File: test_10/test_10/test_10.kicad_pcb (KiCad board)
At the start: 2 copper layers, 100 x 100 mm, 184 parts, among them J2 Array set 0

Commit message: renumber
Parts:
- renumbered H11 to H10, H12 to H11, H13 to H12, H8 to H7, H9 to H8, H10 to H9, J2 to J1, LS49 to LS10, LS21 to LS11, LS22 to LS12, LS23 to LS13, LS24 to LS14, LS25 to LS15, LS26 to LS16, LS27 to LS17, LS28 to LS18, LS50 to LS19, LS30 to LS20, LS11 to LS21, LS12 to LS22, LS13 to LS23, LS14 to LS24, LS15 to LS25, LS16 to LS26, LS17 to LS27, LS18 to LS28, LS19 to LS29, LS20 to LS30, LS41 to LS31, LS80 to LS32, LS47 to LS37, LS48 to LS38, LS51 to LS41, LS52 to LS42, LS53 to LS43, LS54 to LS44, LS55 to LS45, LS56 to LS46, LS57 to LS47, LS58 to LS48, LS59 to LS49, LS60 to LS50, LS71 to LS51, LS72 to LS52, LS73 to LS53, LS74 to LS54, LS75 to LS55, LS79 to LS56, LS78 to LS57, R3 to R1, R12 to R10, R120 to R100, R141 to R101, R142 to R102, R143 to R103, R144 to R104, R145 to R105, R146 to R106, R147 to R107, R151 to R108, R152 to R109, R23 to R11, R153 to R110, R154 to R111, R155 to R112, R156 to R113, R157 to R114, R24 to R12, R25 to R13, R26 to R14, R27 to R15, R28 to R16, R29 to R17, R30 to R18, R31 to R19, R4 to R2, R32 to R20, R43 to R21, R44 to R22, R45 to R23, R46 to R24, R47 to R25, R48 to R26, R49 to R27, R50 to R28, R51 to R29, R5 to R3, R52 to R30, R63 to R31, R64 to R32, R65 to R33, R66 to R34, R67 to R35, R68 to R36, R69 to R37, R70 to R38, R71 to R39, R6 to R4, R72 to R40, R1 to R41, R2 to R42, R13 to R43, R14 to R44, R15 to R45, R16 to R46, R17 to R47, R18 to R48, R19 to R49, R7 to R5, R20 to R50, R21 to R51, R22 to R52, R33 to R53, R34 to R54, R35 to R55, R36 to R56, R37 to R57, R38 to R58, R39 to R59, R8 to R6, R40 to R60, R41 to R61, R42 to R62, R53 to R63, R54 to R64, R55 to R65, R56 to R66, R57 to R67, R58 to R68, R59 to R69, R9 to R7, R60 to R70, R61 to R71, R62 to R72, R10 to R8, R101 to R81, R102 to R82, R103 to R83, R104 to R84, R105 to R85, R106 to R86, R107 to R87, R108 to R88, R109 to R89, R11 to R9, R110 to R90, R111 to R91, R112 to R92, R113 to R93, R114 to R94, R115 to R95, R116 to R96, R117 to R97, R118 to R98, R119 to R99

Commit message: pcb finish
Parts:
- added D1: LED, temp_pcb_lib:CREE_CXB1512, F.Cu at (400.0, 250.0)
- added J2: Array set 0, Connector_Phoenix_MC:PhoenixContact_MCV_1,5_2-G-3.5_1x02_P3.50mm_Vertical, F.Cu at (360.8, 242.0)
- added LS58: Ultrasonic, temp_pcb_lib:Buzzer_MSO-A1040H07T_D10mm_H7mm, F.Cu at (386.1, 285.3)
- added LS59: Ultrasonic, temp_pcb_lib:Buzzer_MSO-A1040H07T_D10mm_H7mm, F.Cu at (375.1, 285.6)
- added R115: 0.1Ω, Resistor_SMD:R_0603_1608Metric, F.Cu at (386.9, 283.0)
- added R116: 0.1Ω, Resistor_SMD:R_0603_1608Metric, F.Cu at (390.3, 288.0)
- added R117: 0.1Ω, Resistor_SMD:R_0603_1608Metric, F.Cu at (375.9, 283.1)
- added R118: 0.1Ω, Resistor_SMD:R_0603_1608Metric, F.Cu at (379.3, 288.4)
- moved R108 174.4 mm to (436.1, 252.5), turned to 180 degrees
- moved R79 172.9 mm to (441.9, 243.6), turned to 180 degrees
- moved R101 172.0 mm to (432.8, 247.4)
- moved R55 167.1 mm to (418.9, 225.9), turned to 180 degrees
- moved R103 166.3 mm to (415.7, 256.2)
- moved R20 162.6 mm to (418.9, 278.8), turned to 180 degrees
- moved R97 157.8 mm to (413.1, 217.1), turned to 180 degrees
- moved R54 157.6 mm to (413.1, 234.7), turned to 180 degrees
- moved R5 152.9 mm to (421.3, 282.9)
- moved R60 152.7 mm to (413.2, 288.0), turned to 180 degrees
- moved R110 151.4 mm to (418.9, 261.2), turned to 180 degrees
- moved R99 149.6 mm to (390.1, 234.7), turned to 180 degrees
- moved R81 148.4 mm to (421.3, 212.1)
- moved R45 146.9 mm to (415.5, 221.0)
- moved R100 146.8 mm to (395.9, 208.0), turned to 180 degrees
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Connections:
- J1 pad 2: Net-(J1-Pad1) -> Net-(J1-Pad2)
- R1 pad 2: Net-(J1-Pad1) -> Net-(J1-Pad2)
- R10 pad 2: Net-(J1-Pad1) -> Net-(J1-Pad2)
- R101 pad 2: Net-(J1-Pad1) -> Net-(J1-Pad2)
- R102 pad 2: Net-(J1-Pad1) -> Net-(J1-Pad2)
- R103 pad 2: Net-(J1-Pad1) -> Net-(J1-Pad2)
- R104 pad 2: Net-(J1-Pad1) -> Net-(J1-Pad2)
- R105 pad 2: Net-(J1-Pad1) -> Net-(J1-Pad2)
- R106 pad 2: Net-(J1-Pad1) -> Net-(J1-Pad2)
- R107 pad 2: Net-(J1-Pad1) -> Net-(J1-Pad2)
- R2 pad 2: Net-(J1-Pad1) -> Net-(J1-Pad2)
- R21 pad 2: Net-(J1-Pad1) -> Net-(J1-Pad2)
- R22 pad 2: Net-(J1-Pad1) -> Net-(J1-Pad2)
- R23 pad 2: Net-(J1-Pad1) -> Net-(J1-Pad2)
- R24 pad 2: Net-(J1-Pad1) -> Net-(J1-Pad2)
- R25 pad 2: Net-(J1-Pad1) -> Net-(J1-Pad2)
- R26 pad 2: Net-(J1-Pad1) -> Net-(J1-Pad2)
- R27 pad 2: Net-(J1-Pad1) -> Net-(J1-Pad2)
- R28 pad 2: Net-(J1-Pad1) -> Net-(J1-Pad2)
- R29 pad 2: Net-(J1-Pad1) -> Net-(J1-Pad2)
- R3 pad 2: Net-(J1-Pad1) -> Net-(J1-Pad2)
- R30 pad 2: Net-(J1-Pad1) -> Net-(J1-Pad2)
- R4 pad 2: Net-(J1-Pad1) -> Net-(J1-Pad2)
- R41 pad 2: Net-(J1-Pad1) -> Net-(J1-Pad2)
- R42 pad 2: Net-(J1-Pad1) -> Net-(J1-Pad2)
- R43 pad 2: Net-(J1-Pad1) -> Net-(J1-Pad2)
- R44 pad 2: Net-(J1-Pad1) -> Net-(J1-Pad2)
- R45 pad 2: Net-(J1-Pad1) -> Net-(J1-Pad2)
- R46 pad 2: Net-(J1-Pad1) -> Net-(J1-Pad2)
- R47 pad 2: Net-(J1-Pad1) -> Net-(J1-Pad2)
- R48 pad 2: Net-(J1-Pad1) -> Net-(J1-Pad2)
- R49 pad 2: Net-(J1-Pad1) -> Net-(J1-Pad2)
- R5 pad 2: Net-(J1-Pad1) -> Net-(J1-Pad2)
- R50 pad 2: Net-(J1-Pad1) -> Net-(J1-Pad2)
- R6 pad 2: Net-(J1-Pad1) -> Net-(J1-Pad2)
- R61 pad 2: Net-(J1-Pad1) -> Net-(J1-Pad2)
- R62 pad 2: Net-(J1-Pad1) -> Net-(J1-Pad2)
- R63 pad 2: Net-(J1-Pad1) -> Net-(J1-Pad2)
- R64 pad 2: Net-(J1-Pad1) -> Net-(J1-Pad2)
- R65 pad 2: Net-(J1-Pad1) -> Net-(J1-Pad2)
- R66 pad 2: Net-(J1-Pad1) -> Net-(J1-Pad2)
- R67 pad 2: Net-(J1-Pad1) -> Net-(J1-Pad2)
- R68 pad 2: Net-(J1-Pad1) -> Net-(J1-Pad2)
- R69 pad 2: Net-(J1-Pad1) -> Net-(J1-Pad2)
- R7 pad 2: Net-(J1-Pad1) -> Net-(J1-Pad2)
- R70 pad 2: Net-(J1-Pad1) -> Net-(J1-Pad2)
- R8 pad 2: Net-(J1-Pad1) -> Net-(J1-Pad2)
- R81 pad 2: Net-(J1-Pad1) -> Net-(J1-Pad2)
- R82 pad 2: Net-(J1-Pad1) -> Net-(J1-Pad2)
- R83 pad 2: Net-(J1-Pad1) -> Net-(J1-Pad2)
- R84 pad 2: Net-(J1-Pad1) -> Net-(J1-Pad2)
- R85 pad 2: Net-(J1-Pad1) -> Net-(J1-Pad2)
- R86 pad 2: Net-(J1-Pad1) -> Net-(J1-Pad2)
- R87 pad 2: Net-(J1-Pad1) -> Net-(J1-Pad2)
- R88 pad 2: Net-(J1-Pad1) -> Net-(J1-Pad2)
- R89 pad 2: Net-(J1-Pad1) -> Net-(J1-Pad2)
- R9 pad 2: Net-(J1-Pad1) -> Net-(J1-Pad2)
- R90 pad 2: Net-(J1-Pad1) -> Net-(J1-Pad2)
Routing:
- net Net-(J1-Pad2): track 0.00 -> 81.0 mm, vias 0 -> 59
- net Net-(D1-Pad1): track 0.00 -> 55.3 mm
- net Net-(D1-Pad2): track 0.00 -> 34.5 mm
- net Net-(LS59-Pad2): track 0.00 -> 2.81 mm
- net Net-(LS38-Pad1): track 0.00 -> 2.76 mm
- net Net-(LS37-Pad2): track 0.00 -> 2.76 mm
- net Net-(LS30-Pad2): track 0.00 -> 2.76 mm
- net Net-(LS58-Pad2): track 0.00 -> 2.71 mm
- net Net-(LS50-Pad1): track 0.00 -> 2.71 mm
- net Net-(LS13-Pad1): track 0.00 -> 2.71 mm
- net Net-(LS5-Pad2): track 0.00 -> 2.70 mm
- net Net-(LS28-Pad1): track 0.00 -> 2.68 mm
- net Net-(LS21-Pad1): track 0.00 -> 2.68 mm
- net Net-(LS15-Pad1): track 0.00 -> 2.68 mm
- net Net-(LS29-Pad1): track 0.00 -> 2.63 mm
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- added copper zone on F.Cu, net Net-(J1-Pad1)
- added copper zone on B.Cu, net Net-(J1-Pad2)

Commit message: 3 trans mas
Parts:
- added LS60: Ultrasonic, temp_pcb_lib:Buzzer_MSO-A1040H07T_D10mm_H7mm, F.Cu at (391.8, 294.1)
- added LS61: Ultrasonic, temp_pcb_lib:Buzzer_MSO-A1040H07T_D10mm_H7mm, F.Cu at (403.3, 294.1)
- added LS62: Ultrasonic, temp_pcb_lib:Buzzer_MSO-A1040H07T_D10mm_H7mm, F.Cu at (358.3, 240.5)
- added R119: 0.1Ω, Resistor_SMD:R_0603_1608Metric, F.Cu at (392.7, 291.6)
- added R120: 0.1Ω, Resistor_SMD:R_0603_1608Metric, F.Cu at (404.2, 291.6)
- added R121: 0.1Ω, Resistor_SMD:R_0603_1608Metric, F.Cu at (359.1, 237.9)
- added R122: 0.1Ω, Resistor_SMD:R_0603_1608Metric, F.Cu at (397.6, 291.6)
- added R123: 0.1Ω, Resistor_SMD:R_0603_1608Metric, F.Cu at (409.1, 291.6)
- added R124: 0.1Ω, Resistor_SMD:R_0603_1608Metric, F.Cu at (364.7, 243.2)
- J1, J2: moved to B.Cu
- moved J2 3.95 mm to (361.4, 245.9), turned to 180 degrees
- turned J1 to 270 degrees
- renumbered R115 to R108, R117 to R109, R108 to R110, R109 to R111, R110 to R112, R111 to R113, R112 to R114, R113 to R115, R114 to R116, R116 to R117
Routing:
- net Net-(D1-Pad2): track 34.5 -> 42.1 mm
- net Net-(J1-Pad2): track 81.0 -> 85.1 mm, vias 59 -> 62
- net Net-(LS62-Pad1): track 0.00 -> 2.61 mm
- net Net-(LS61-Pad1): track 0.00 -> 2.53 mm
- net Net-(LS60-Pad1): track 0.00 -> 2.53 mm
- net Net-(LS61-Pad2): track 0.00 -> 2.51 mm
- net Net-(LS60-Pad2): track 0.00 -> 2.51 mm
- net Net-(LS62-Pad2): track 0.00 -> 2.45 mm
- net Net-(D1-Pad1): track 55.3 -> 53.3 mm

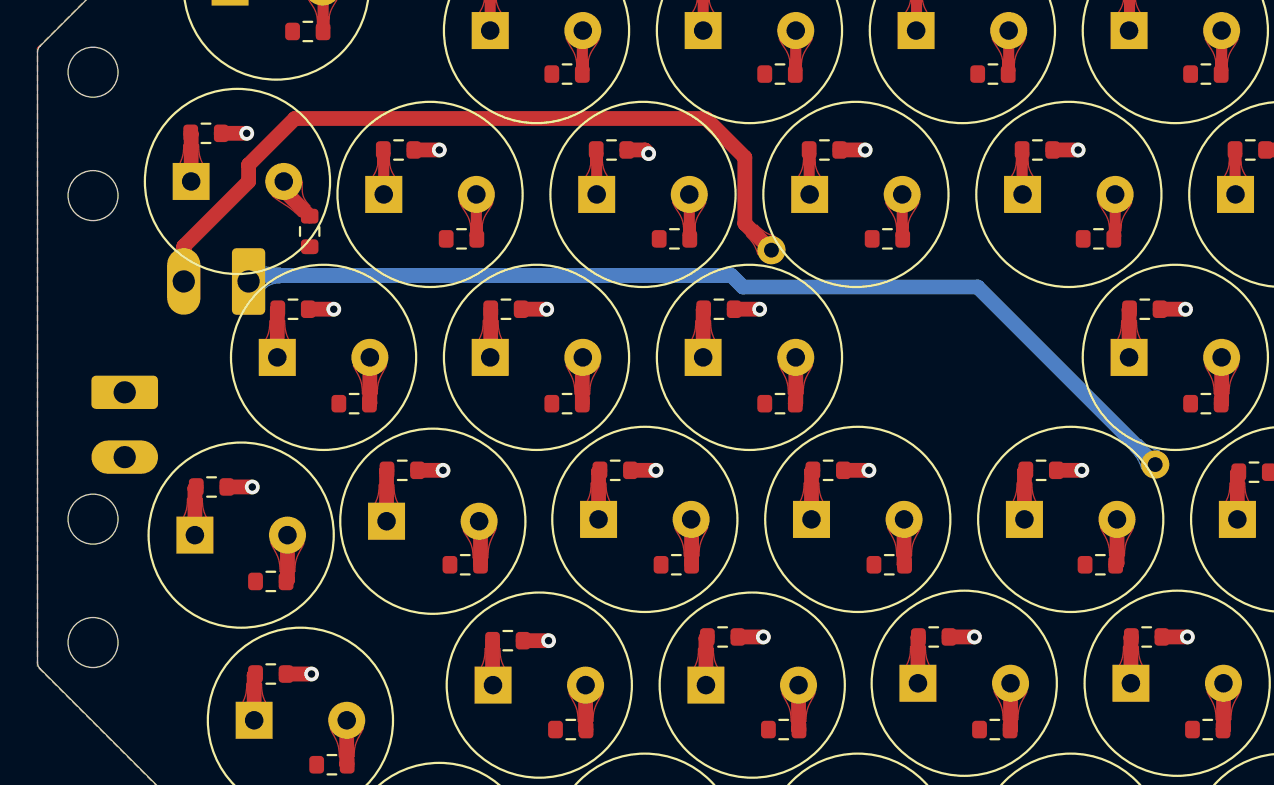
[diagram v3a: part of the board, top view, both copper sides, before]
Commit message: bracket alignement
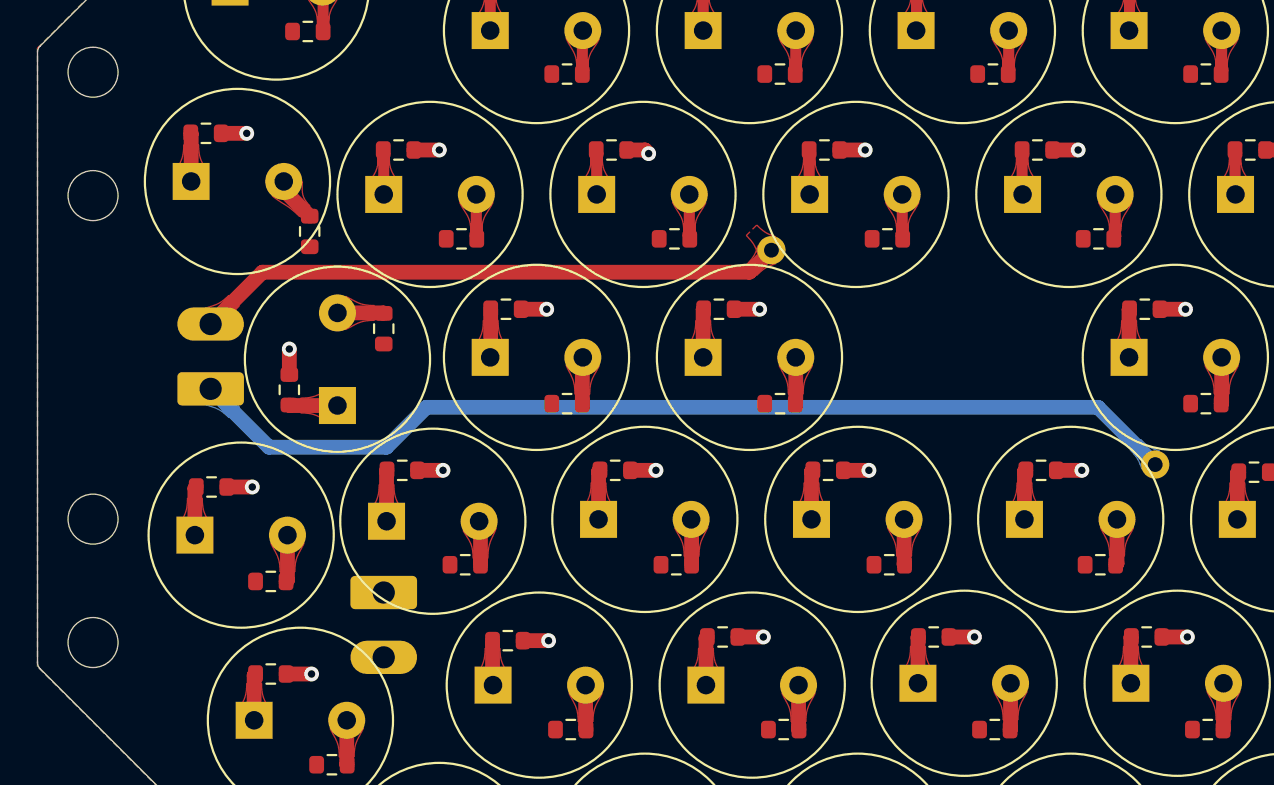
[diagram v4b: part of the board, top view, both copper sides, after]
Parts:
- moved J1 17.7 mm to (368.7, 262.7)
- moved J2 6.15 mm to (359.4, 251.7), turned to 90 degrees
- moved R56 4.35 mm to (368.7, 248.4), turned to 270 degrees
- moved R46 4.35 mm to (363.6, 251.8), turned to 90 degrees
- moved LS26 4.16 mm to (366.2, 252.6), turned to 90 degrees
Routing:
- net Net-(D1-Pad2): track 42.1 -> 31.9 mm
- net Net-(D1-Pad1): track 53.3 -> 54.5 mm
